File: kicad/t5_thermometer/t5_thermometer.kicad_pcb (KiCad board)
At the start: 2 copper layers, 27 x 27 mm, 15 parts, among them J1 Conn_ARM_JTAG_SWD_10, J2 UART_DBG, J4 Screw_Terminal_01x06, U1 STM32F042F6Px, U2 TSR_1-2433

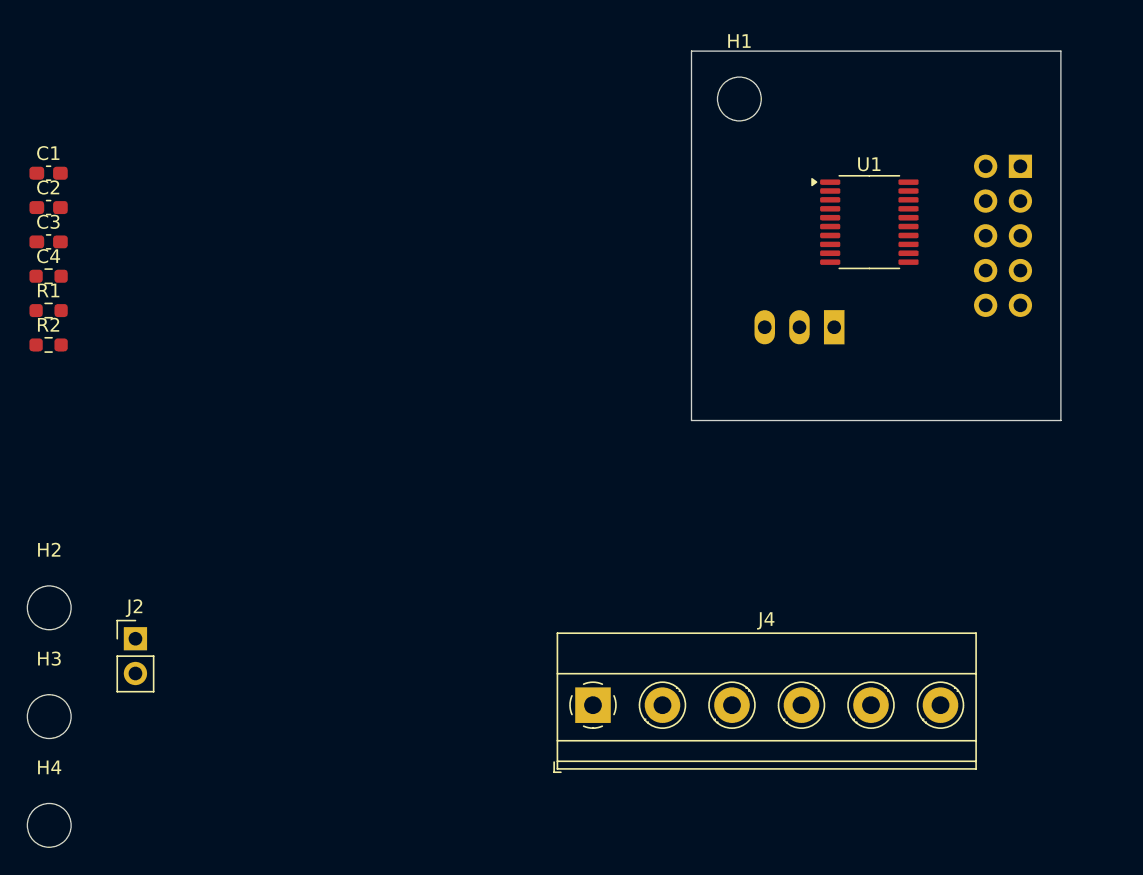
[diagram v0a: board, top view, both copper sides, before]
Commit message: Add configuration and PCB design which was ordered.
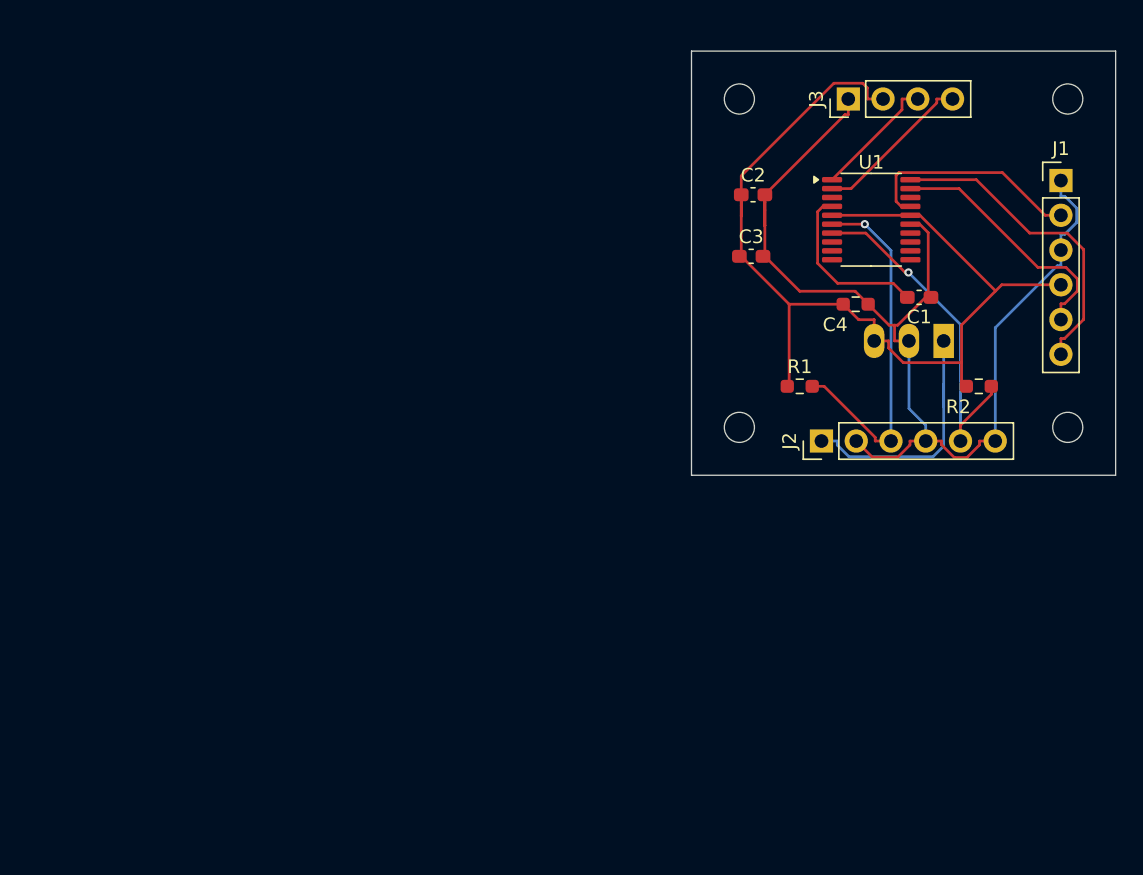
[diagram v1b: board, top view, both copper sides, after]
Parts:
- removed J4: Screw_Terminal_01x06, TerminalBlock_Phoenix:TerminalBlock_Phoenix_MKDS-1,5-6-5.08_1x06_P5.08mm_Horizontal
- added J3: Display, Connector_PinHeader_2.54mm:PinHeader_1x04_P2.54mm_Vertical, F.Cu at (185.5, 87.0)
- H1, H2, H3, H4: footprint MountingHole:MountingHole_3.2mm_M3 -> MountingHole:MountingHole_2.2mm_M2
- J1: value Conn_ARM_JTAG_SWD_10 -> DBG; footprint Connector_PinHeader_2.54mm:PinHeader_2x05_P2.54mm_Vertical -> Connector_PinHeader_2.54mm:PinHeader_1x06_P2.54mm_Vertical; moved to F.Cu
- J2: value UART_DBG -> ~; footprint Connector_PinHeader_2.54mm:PinHeader_1x02_P2.54mm_Vertical -> Connector_PinHeader_2.54mm:PinHeader_1x06_P2.54mm_Vertical
- moved H2 83.2 mm to (201.5, 87.0)
- moved H4 79.9 mm to (201.5, 111.0)
- moved R2 68.1 mm to (195.0, 108.0), turned to 180 degrees
- moved C1 64.3 mm to (190.6, 101.5), turned to 180 degrees
- moved C4 59.0 mm to (186.0, 102.0), turned to 180 degrees
- moved R1 55.2 mm to (181.9, 108.0)
- moved H3 54.7 mm to (177.5, 111.0)
- moved J2 52.2 mm to (183.5, 112.0), turned to 90 degrees
- moved C2 51.5 mm to (178.5, 94.0)
- moved C3 51.4 mm to (178.4, 98.5)
- moved U2 8.06 mm to (192.4, 104.7)
- moved J1 3.14 mm to (201.0, 93.0), turned to 0 degrees
- moved U1 0.22 mm to (187.1, 95.8)
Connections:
- C1 pad 2: Net-(J1-~{RESET}) -> Net-(U1-NRST)
- J1 pad 1: +3.3V -> GND
- J1 pad 2: /SYS_SWDIO -> /USART1_TX_DBG
- J1 pad 4: /SYS_SWCLK -> +3.3V
- J1 pad 5: GND -> /SYS_SWDIO
- J1 pad 6: GND -> /SYS_SWCLK
- J2 pad 1: /USART1_TX_DBG -> Net-(J2-Pin_1)
- U1 pad 2: unconnected-(U1-PF0-Pad2) -> /I2C_SDA_DISPLAY
- U1 pad 3: /I2C_SDA_DISPLAY -> unconnected-(U1-PF1-Pad3)
- U1 pad 4: Net-(J1-~{RESET}) -> Net-(U1-NRST)
- U2 pad 1: Net-(J4-Pin_1) -> Net-(J2-Pin_1)
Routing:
- net GND: track 0.00 -> 83.3 mm
- net +3.3V: track 0.00 -> 75.6 mm
- net /ADC_INDOOR: track 0.00 -> 26.6 mm, vias 0 -> 1
- net /ADC_OUTDOOR: track 0.00 -> 25.8 mm, vias 0 -> 1
- net /SYS_SWCLK: track 0.00 -> 23.3 mm
- net Net-(J2-Pin_1): track 0.00 -> 19.2 mm
- net /SYS_SWDIO: track 0.00 -> 18.6 mm
- net /USART1_TX_DBG: track 0.00 -> 16.5 mm
- net Net-(U1-NRST): track 0.00 -> 12.6 mm
- net /I2C_SDA_DISPLAY: track 0.00 -> 11.7 mm
- net /I2C_SCL_DISPLAY: track 0.00 -> 9.17 mm
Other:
- board size 27 x 27 mm -> 31 x 31 mm
- board text added: "3.3V"
- board text added: "ADC_INDOOR"
- board text added: "ADC_OUTDOOR"
- board text added: "GND"
- board text added: "SYS_SWCLK"
- board text added: "SYS_SWDIO"
- board text added: "UART_TX_DBG"
- board text added: "V_BAT"

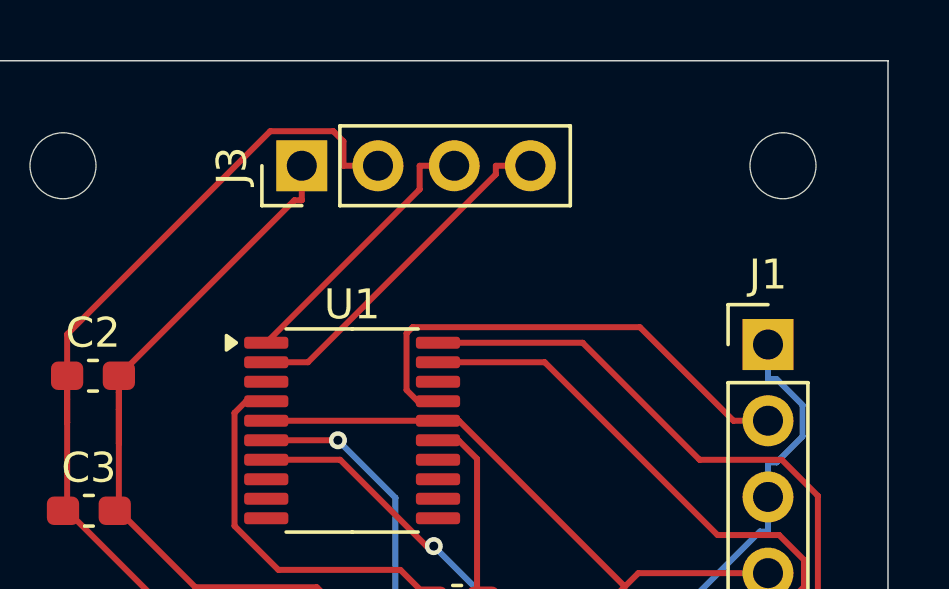
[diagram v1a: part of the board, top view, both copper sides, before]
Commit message: schematic change: - Add 4,7k pull up for I2C - Connect PB8 to GND. PB8 was initially planned as I2C SCL, but due to   the fact that it also operates as BOOT0 pin, it cannot be pulled up.
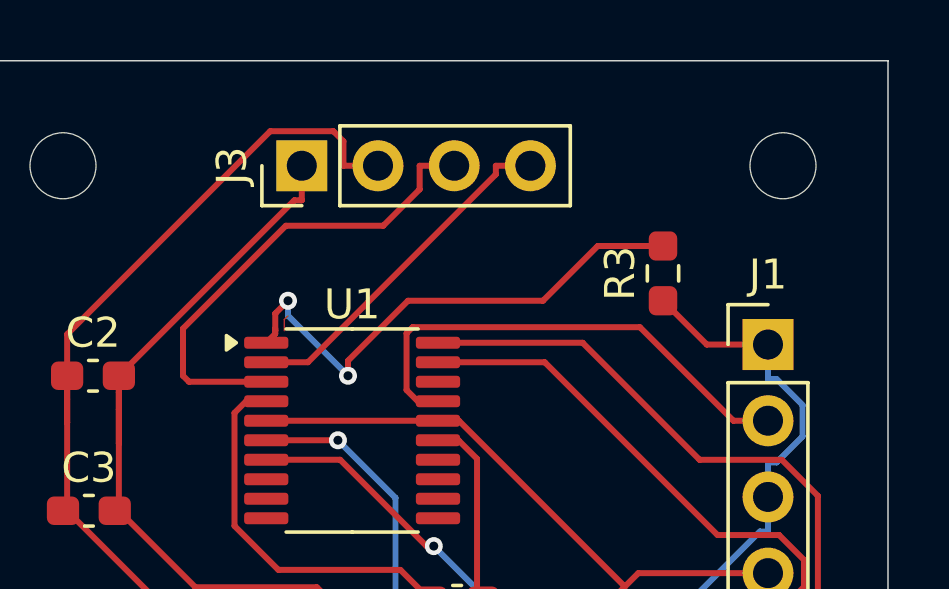
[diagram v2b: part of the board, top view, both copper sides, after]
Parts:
- added R3: R10k, Resistor_SMD:R_0603_1608Metric_Pad0.98x0.95mm_HandSolder, F.Cu at (197.5, 90.6)
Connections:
- U1 pad 1: /I2C_SCL_DISPLAY -> Net-(U1-PB8)
- U1 pad 3: unconnected-(U1-PF1-Pad3) -> /I2C_SCL_DISPLAY
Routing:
- net Net-(U1-PB8): track 0.00 -> 17.7 mm, vias 0 -> 2
- net /I2C_SCL_DISPLAY: track 9.17 -> 16.2 mm
- net GND: track 83.3 -> 87.4 mm
- net (no net): track 0.00 -> 0.55 mm

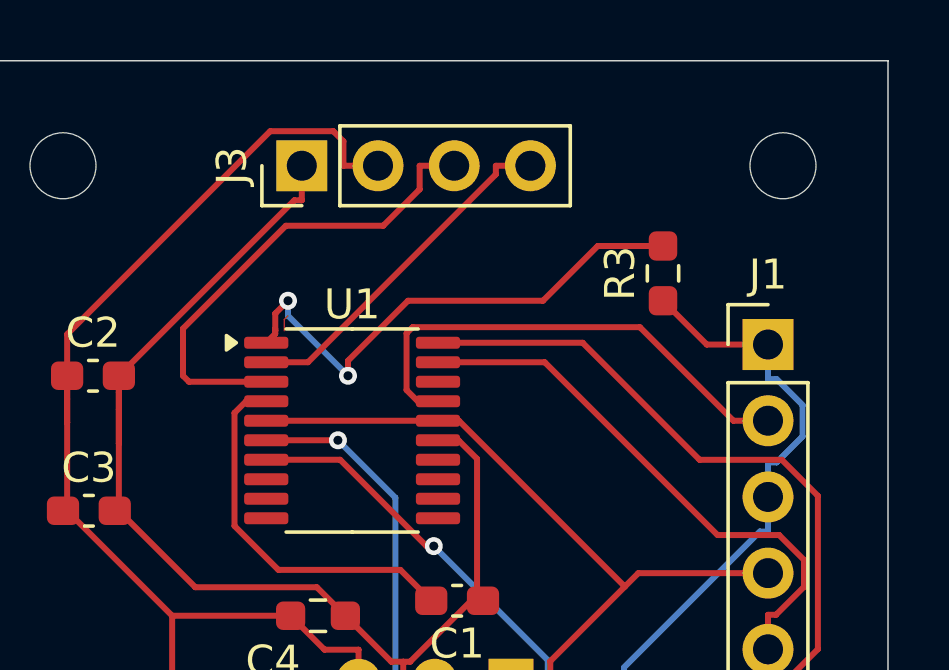
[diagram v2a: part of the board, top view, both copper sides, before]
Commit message: Change Layout to match the current working status: BOOT0 is now connected to GND
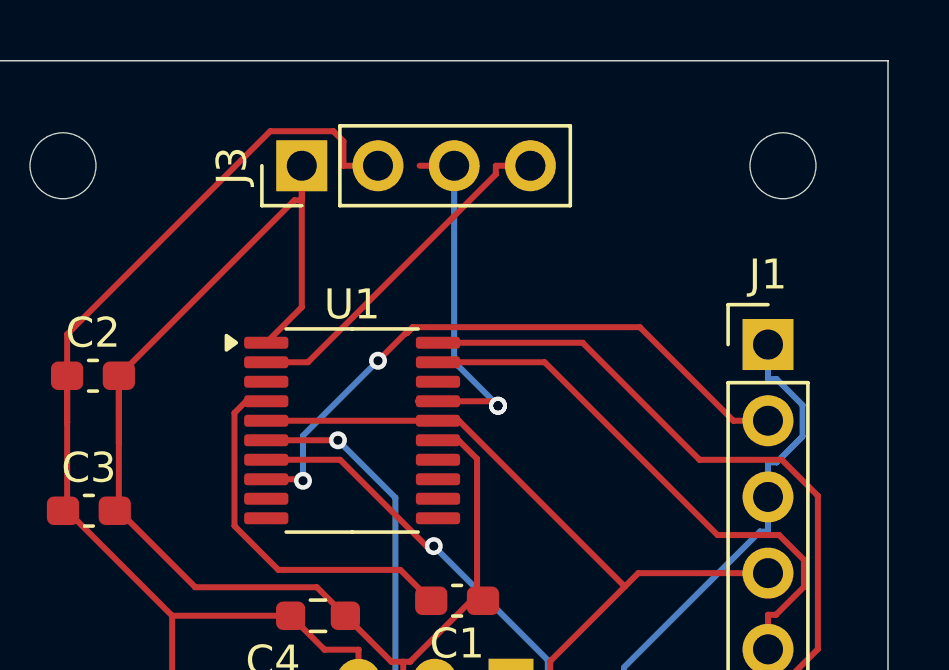
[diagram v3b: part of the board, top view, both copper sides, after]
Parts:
- removed R3: R10k, Resistor_SMD:R_0603_1608Metric_Pad0.98x0.95mm_HandSolder
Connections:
- J1 pad 2: /USART1_TX_DBG -> /USART2_TX_DBG
- U1 pad 1: Net-(U1-PB8) -> GND
- U1 pad 17: /USART1_TX_DBG -> /I2C_SCL_DISPLAY
- U1 pad 3: /I2C_SCL_DISPLAY -> unconnected-(U1-PF1-Pad3)
- U1 pad 8: unconnected-(U1-PA2-Pad8) -> /USART2_TX_DBG
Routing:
- net /USART2_TX_DBG: track 0.00 -> 21.2 mm, vias 0 -> 2
- net Net-(U1-PB8): track 17.7 -> 0.00 mm, vias 2 -> 0
- net /USART1_TX_DBG: track 16.5 -> 0.00 mm
- net /I2C_SCL_DISPLAY: track 16.2 -> 12.5 mm, vias 0 -> 2
- net GND: track 87.4 -> 89.7 mm
- net (no net): track 0.55 -> 0.00 mm
